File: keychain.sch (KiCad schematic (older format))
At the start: 17 parts, among them P1 USB_OTG, P2 VBAT, P3 CONN_01X04, Q1 FDN340P, SW1 BUTTON_SMALL, U1 EFM32HG308

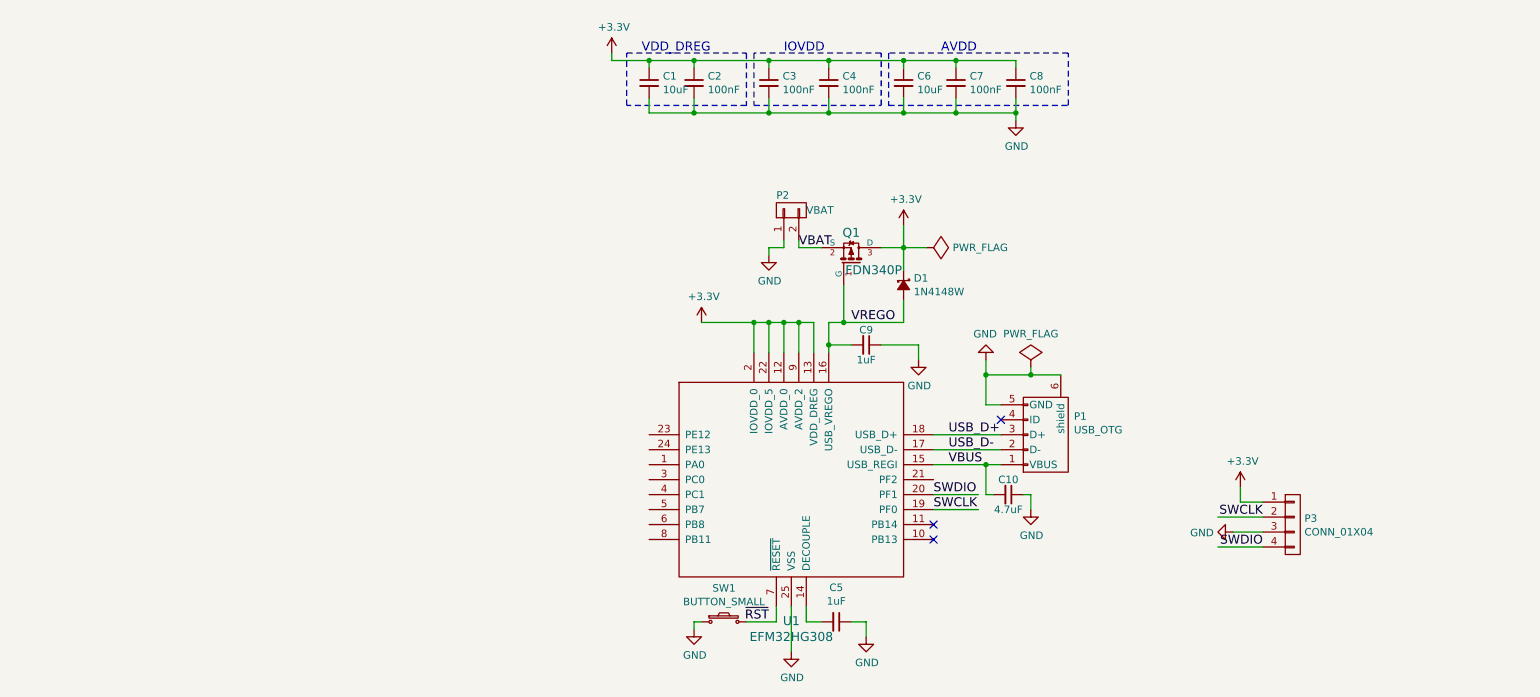
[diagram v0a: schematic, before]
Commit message: Switched to EFM32TG110, redid board layout
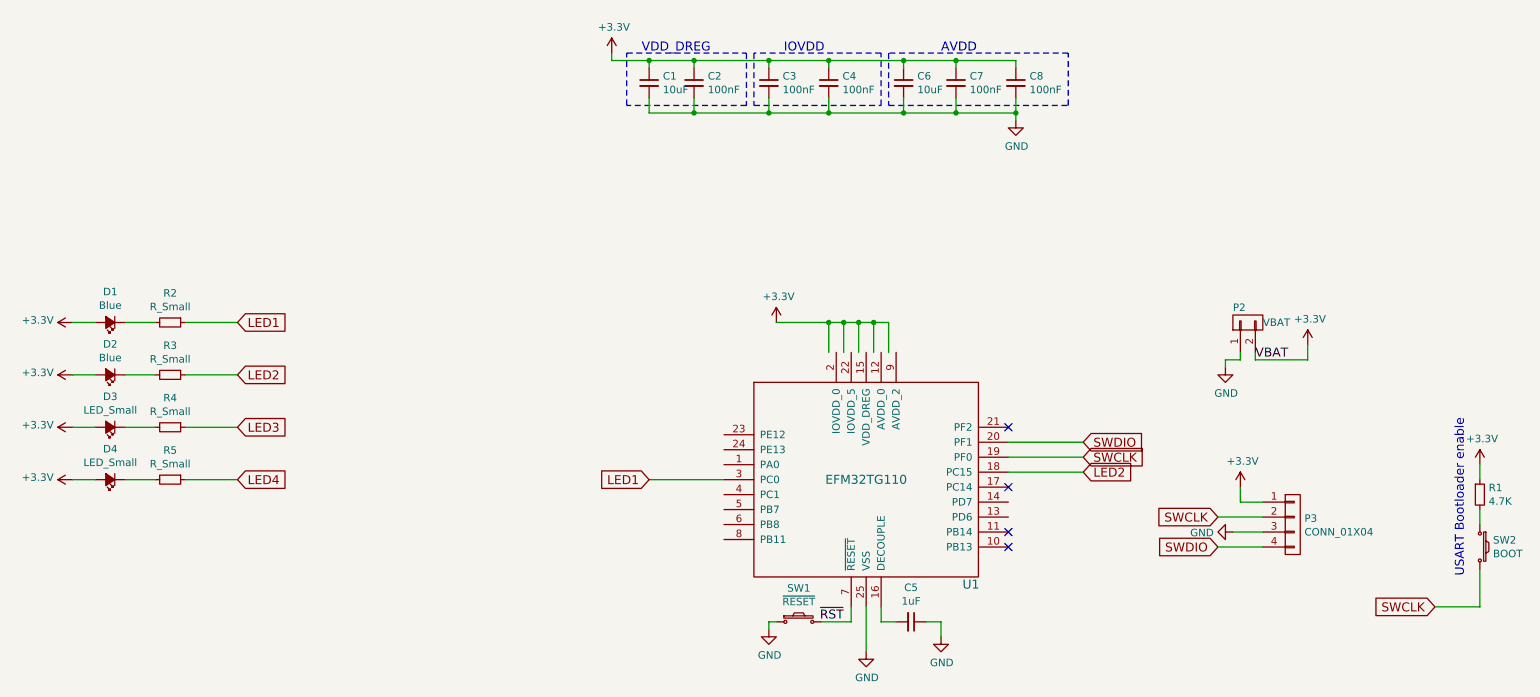
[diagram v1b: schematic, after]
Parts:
- removed C10: 4.7uF, Capacitors_SMD:C_0603, symbol C_Small
- removed C9: 1uF, Capacitors_SMD:C_0603, symbol C_Small
- removed D1: 1N4148W, Diodes_SMD:SOD-123, symbol D_Schottky_Small
- removed P1: USB_OTG, Connect:USB_Micro-B_10103594-0001LF, symbol USB_OTG
- removed Q1: FDN340P, TO_SOT_Packages_SMD:SOT-23, symbol FDN340P
- removed U1: EFM32HG308, Housings_DFN_QFN:QFN-24-1EP_5x5mm_Pitch0.65mm, symbol EFM32HG308
- added D1, D2: Blue, LEDs:LED_0603, symbol LED_Small
- added D3, D4: LED_Small, LEDs:LED_0603, symbol LED_Small
- added R1: 4.7K, Resistors_SMD:R_0603, symbol R_Small
- added R2, R3, R4, R5: R_Small, Resistors_SMD:R_0603, symbol R_Small
- added SW2: BOOT, Buttons_Switches_SMD:SW_SPST_B3U-1000P, symbol BUTTON_SMALL
- added U1: EFM32TG110, Housings_DFN_QFN:QFN-24-1EP_5x5mm_Pitch0.65mm, symbol EFM32TG110
- P3: footprint Pin_Headers:Pin_Header_Straight_1x04_Pitch2.00mm -> Pin_header_extra:CONN_01X04_1.27mm
- SW1: value BUTTON_SMALL -> ~RESET~
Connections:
- net labels added: LED1, LED2, LED3, LED4
- net labels removed: USB_D+, USB_D-, VBUS, VREGO
- wire segments 64 -> 63
- no-connect marks 3 -> 4
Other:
- note added: "USART Bootloader enable"
- moved on the sheet: C5, P2, SW1

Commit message: More or less done.
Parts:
- removed C4: 100nF, Capacitors_SMD:C_0603, symbol C_Small
- added L1: BLM21B102S, Capacitors_SMD:C_0805, symbol INDUCTOR_Small
- added P1: CAP_SLIDER, capsense:slider_2p, symbol CONN_01X02
- added R6: 1R, Resistors_SMD:R_0603, symbol R_Small
- added R7, R8: 100R, Resistors_SMD:R_0603, symbol R_Small
- C7, C8: value 100nF -> 10nF
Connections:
- net labels added: CAP_S_1, CAP_S_2, VDDA
- wire segments 63 -> 77
- no-connect marks 4 -> 9
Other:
- moved on the sheet: C6, C7, C8, D1, D2, D3, D4, R2, R3, R4, R5

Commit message: Moar changes
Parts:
- added P4: CONN_01X05, Pin_header_extra:CONN_01X05_SMDISH, symbol CONN_01X05
- added SW3: USR1, smallbutton:SmallButton, symbol SW_PUSH_Small_Horizontal
- added SW4: USR2, smallbutton:SmallButton, symbol SW_PUSH_Small_Horizontal
- SW1, SW2: footprint Buttons_Switches_SMD:SW_SPST_B3U-1000P -> smallbutton:Tactile_Push_Button_SMD_3x3x1.5mm.kicad_mod
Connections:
- net CAP_S_1: now also U1.18 (PC15); no longer U1.4 (PC1)
- net GND: now also P4.1 (P1), SW3.1, SW4.2
- net LED1: now also U1.23 (PE12); no longer U1.24 (PE13)
- net LED3: now also U1.14 (PD7); no longer U1.13 (PD6)
- net at U1.1 (PA0): now also SW3.2
- net at U1.3 (PC0): now also P4.5 (P5)
- net at U1.5 (PB7): now also P4.3 (P3)
- net at U1.6 (PB8): now also P4.2 (P2)
- new net: SW4.1, U1.13 (PD6)
- new net: P4.4 (P4), U1.4 (PC1)
- no-connect marks 9 -> 3
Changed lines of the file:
@@
 Wire Wire Line
 	8800 2750 8800 2800
-Wire Wire Line
-	8800 2800 9250 2800
 Text Label 8800 2800 0    60   ~ 0
 VBAT
@@
 F 0 "SW1" H 5750 4775 50  0000 C CNN
 F 1 "~RESET~" H 5750 4684 50  0000 C CNN
-F 2 "Buttons_Switches_SMD:SW_SPST_B3U-1000P" H 5750 4550 50  0001 C CNN
+F 2 "smallbutton:Tactile_Push_Button_SMD_3x3x1.5mm.kicad_mod" H 5750 4550 50  0001 C CNN
 F 3 "" H 5750 4550 50  0000 C CNN
 	1    5750 4550
@@
 L +3.3V #PWR010
 U 1 1 5825CA51
-P 9150 2700
-F 0 "#PWR010" H 9150 2550 50  0001 C CNN
-F 1 "+3.3V" H 9165 2873 50  0000 C CNN
-F 2 "" H 9150 2700 50  0000 C CNN
-F 3 "" H 9150 2700 50  0000 C CNN
-	1    9150 2700
-	1    0    0    -1
-$EndComp
-Wire Wire Line
-	9150 2800 9150 2700
+P 8950 2700
+F 0 "#PWR010" H 8950 2550 50  0001 C CNN
+F 1 "+3.3V" H 8965 2873 50  0000 C CNN
+F 2 "" H 8950 2700 50  0000 C CNN
+F 3 "" H 8950 2700 50  0000 C CNN
+	1    8950 2700
+	1    0    0    -1
+$EndComp
 $Comp
 L BUTTON_SMALL SW2
@@
 F 0 "SW2" V 10254 4138 50  0000 L CNN
 F 1 "BOOT" V 10345 4138 50  0000 L CNN
-F 2 "Buttons_Switches_SMD:SW_SPST_B3U-1000P" H 10300 4050 50  0001 C CNN
+F 2 "smallbutton:Tactile_Push_Button_SMD_3x3x1.5mm.kicad_mod" H 10300 4050 50  0001 C CNN
 F 3 "" H 10300 4050 50  0000 C CNN
 	1    10300 4050
@@
 Text GLabel 2000 3600 2    60   Input ~ 0
 LED4
-Text GLabel 4750 3400 0    60   Input ~ 0
+Text GLabel 4750 3300 0    60   Input ~ 0
 LED1
-Wire Wire Line
-	5250 3400 4750 3400
 Text GLabel 7650 3250 2    60   Input ~ 0
 LED2
@@
 	7150 3650 7650 3650
 Wire Wire Line
-	5250 3700 4750 3700
-Text GLabel 4750 3700 0    60   Input ~ 0
+	7150 3550 7650 3550
+Text GLabel 7650 3550 2    60   Input ~ 0
 CAP_S_1
 Text GLabel 4700 4000 0    60   Input ~ 0
@@
 Wire Wire Line
 	5250 4000 4700 4000
-Text GLabel 7700 3850 2    60   Input ~ 0
+Text GLabel 7700 3750 2    60   Input ~ 0
 LED3
 Wire Wire Line
-	7700 3850 7150 3850
-NoConn ~ 7150 3750
+	7700 3750 7150 3750
 Wire Wire Line
 	5050 1050 5050 1150
@@
 	1    0    0    -1
 $EndComp
-NoConn ~ 7150 3550
-NoConn ~ 5250 3900
-NoConn ~ 5250 3800
-NoConn ~ 5250 3600
-NoConn ~ 5250 3500
-NoConn ~ 5250 3300
+NoConn ~ 5250 3400
 $Comp
 L PWR_FLAG #FLG019
 U 1 1 5827846A
-P 9250 2800
-F 0 "#FLG019" H 9250 2895 50  0001 C CNN
-F 1 "PWR_FLAG" V 9250 2978 50  0000 L CNN
-F 2 "" H 9250 2800 50  0000 C CNN
-F 3 "" H 9250 2800 50  0000 C CNN
-	1    9250 2800
-	0    1    1    0
-$EndComp
-Connection ~ 9150 2800
+P 9100 2800
+F 0 "#FLG019" H 9100 2895 50  0001 C CNN
+F 1 "PWR_FLAG" V 9100 2978 50  0000 L CNN
+F 2 "" H 9100 2800 50  0000 C CNN
+F 3 "" H 9100 2800 50  0000 C CNN
+	1    9100 2800
+	0    1    1    0
+$EndComp
 Wire Wire Line
 	5850 2550 6200 2550
@@
 	1    0    0    -1
 $EndComp
+Wire Wire Line
+	5250 3300 4750 3300
+$Comp
+L CONN_01X05 P4
+U 1 1 58276AA7
+P 3950 3800
+F 0 "P4" H 3869 3375 50  0000 C CNN
+F 1 "CONN_01X05" H 3869 3466 50  0000 C CNN
+F 2 "Pin_header_extra:CONN_01X05_SMDISH" H 3950 3800 50  0001 C CNN
+F 3 "" H 3950 3800 50  0000 C CNN
+	1    3950 3800
+	-1   0    0    1
+$EndComp
+Wire Wire Line
+	5250 3900 4150 3900
+Wire Wire Line
+	5250 3800 4150 3800
+Wire Wire Line
+	5250 3700 4150 3700
+Wire Wire Line
+	5250 3600 4150 3600
+$Comp
+L GND #PWR023
+U 1 1 58276E33
+P 4250 4100
+F 0 "#PWR023" H 4250 3850 50  0001 C CNN
+F 1 "GND" H 4255 3927 50  0000 C CNN
+F 2 "" H 4250 4100 50  0000 C CNN
+F 3 "" H 4250 4100 50  0000 C CNN
+	1    4250 4100
+	1    0    0    -1
+$EndComp
+Wire Wire Line
+	4150 4000 4250 4000
+Wire Wire Line
+	4250 4000 4250 4100
+Wire Wire Line
+	8800 2800 9100 2800
+Wire Wire Line
+	8950 2700 8950 2800
+Connection ~ 8950 2800
+$Comp
+L SW_PUSH_Small_Horizontal SW3
+U 1 1 5827923C
+P 5000 3500
+F 0 "SW3" H 5000 3600 50  0000 C CNN
+F 1 "USR1" H 5000 3450 50  0000 C CNN
+F 2 "smallbutton:SmallButton" H 5000 3634 50  0000 C CNN
+F 3 "" H 5000 3700 50  0000 C CNN
+	1    5000 3500
+	1    0    0    -1
+$EndComp
+$Comp
+L GND #PWR024
+U 1 1 582798BF
+P 4700 3500
+F 0 "#PWR024" H 4700 3250 50  0001 C CNN
+F 1 "GND" V 4705 3372 50  0000 R CNN
+F 2 "" H 4700 3500 50  0000 C CNN
+F 3 "" H 4700 3500 50  0000 C CNN
+	1    4700 3500
+	0    1    1    0
+$EndComp
+Wire Wire Line
+	4850 3500 4700 3500
+Wire Wire Line
+	5150 3500 5250 3500
+$Comp
+L SW_PUSH_Small_Horizontal SW4
+U 1 1 5827A278
+P 7500 3850
+F 0 "SW4" H 7350 3900 50  0000 R CNN
+F 1 "USR2" H 7600 3800 50  0000 R CNN
+F 2 "smallbutton:SmallButton" H 8100 3550 50  0000 R CNN
+F 3 "" H 7500 4050 50  0000 C CNN
+	1    7500 3850
+	1    0    0    -1
+$EndComp
+$Comp
+L GND #PWR025
+U 1 1 5827A27E
+P 7800 3850
+F 0 "#PWR025" H 7800 3600 50  0001 C CNN
+F 1 "GND" V 7805 3722 50  0000 R CNN
+F 2 "" H 7800 3850 50  0000 C CNN
+F 3 "" H 7800 3850 50  0000 C CNN
+	1    7800 3850
+	0    -1   -1   0
+$EndComp
+Wire Wire Line
+	7800 3850 7650 3850
+Wire Wire Line
+	7150 3850 7350 3850
 $EndSCHEMATC

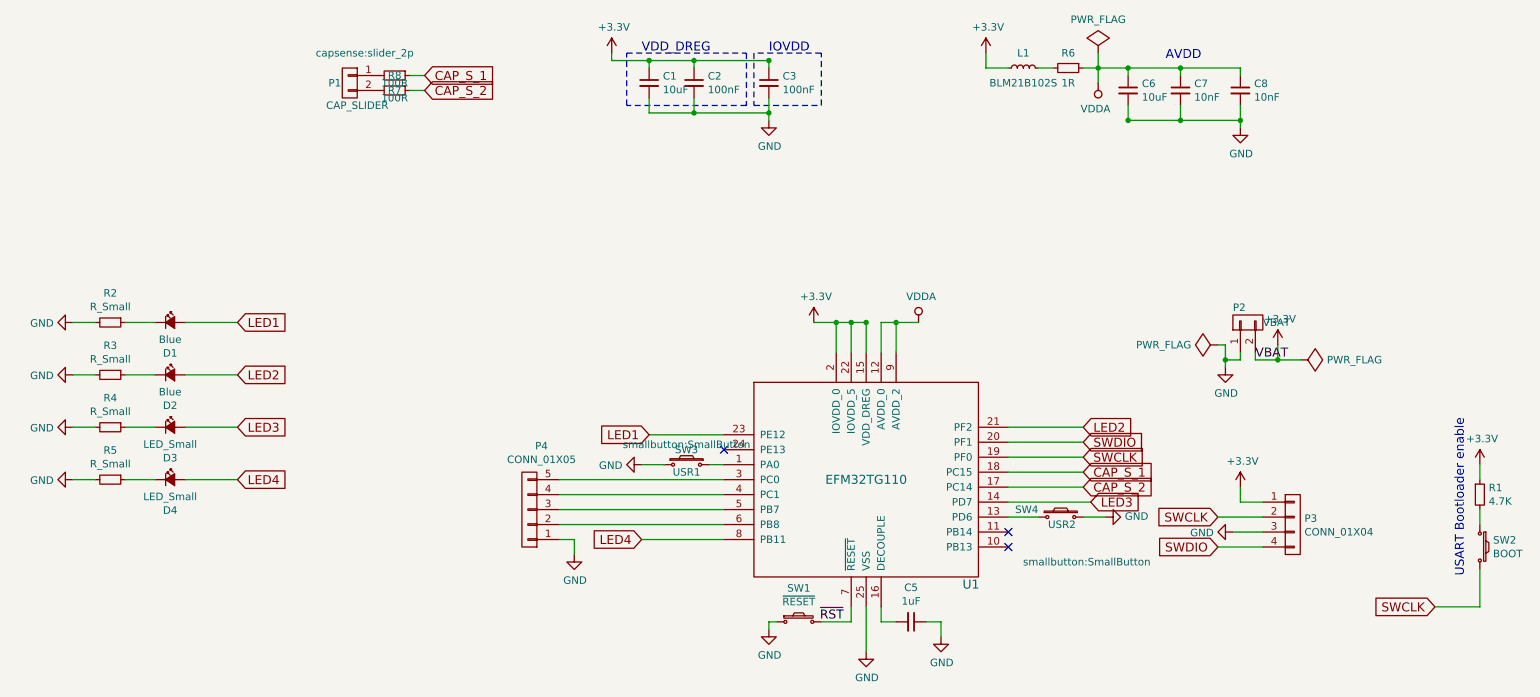
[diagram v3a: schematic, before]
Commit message: Add 0R resistor for measuring current
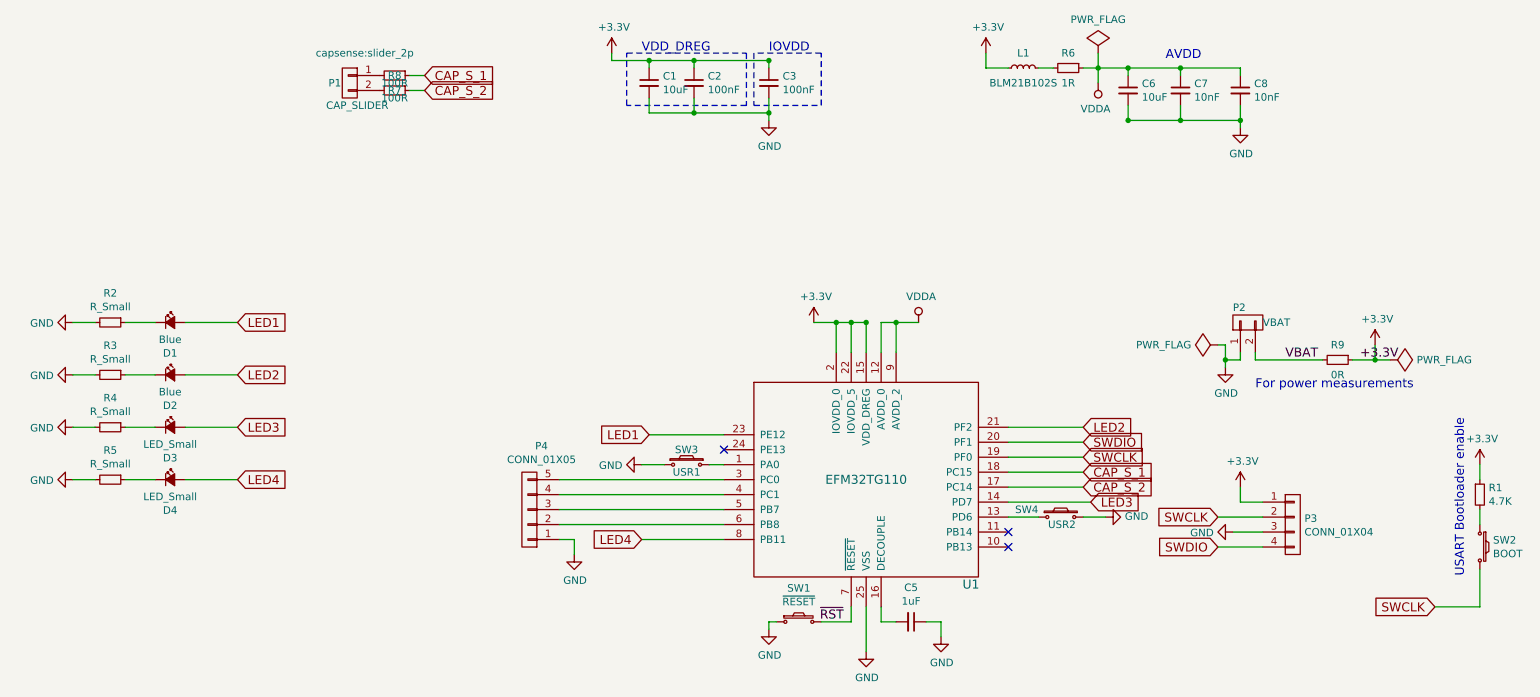
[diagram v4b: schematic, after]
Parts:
- added R9: 0R, Resistors_SMD:R_0603, symbol R_Small
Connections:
- net +3V3: now also R9.1; no longer P2.2 (P2)
- new net VBAT: P2.2 (P2), R9.2
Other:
- note added: "For power measurements"

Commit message: Rotate buttons to look nicer, fix missing reset connection
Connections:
- net US1_TX: now reaches P4.5 (P5), U1.3 (PC0)
- net US1_RX: now reaches P4.4 (P4), U1.4 (PC1)
- net US1_CLK: now reaches P4.3 (P3), U1.5 (PB7)
- net US1_CS: now reaches P4.2 (P2), U1.6 (PB8)
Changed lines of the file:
@@
 Text Label 9500 2800 0    60   ~ 0
 +3.3V
+Text Label 4500 3600 0    60   ~ 0
+US1_TX
+Text Label 4500 3700 0    60   ~ 0
+US1_RX
+Text Label 4500 3800 0    60   ~ 0
+US1_CLK
+Text Label 4500 3900 0    60   ~ 0
+US1_CS
 $EndSCHEMATC
